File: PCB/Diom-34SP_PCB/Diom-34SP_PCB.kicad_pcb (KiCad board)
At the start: 2 copper layers, 119.9 x 95.5 mm, 19 parts, among them J1 Conn_01x02_Male, U1 nice_nano

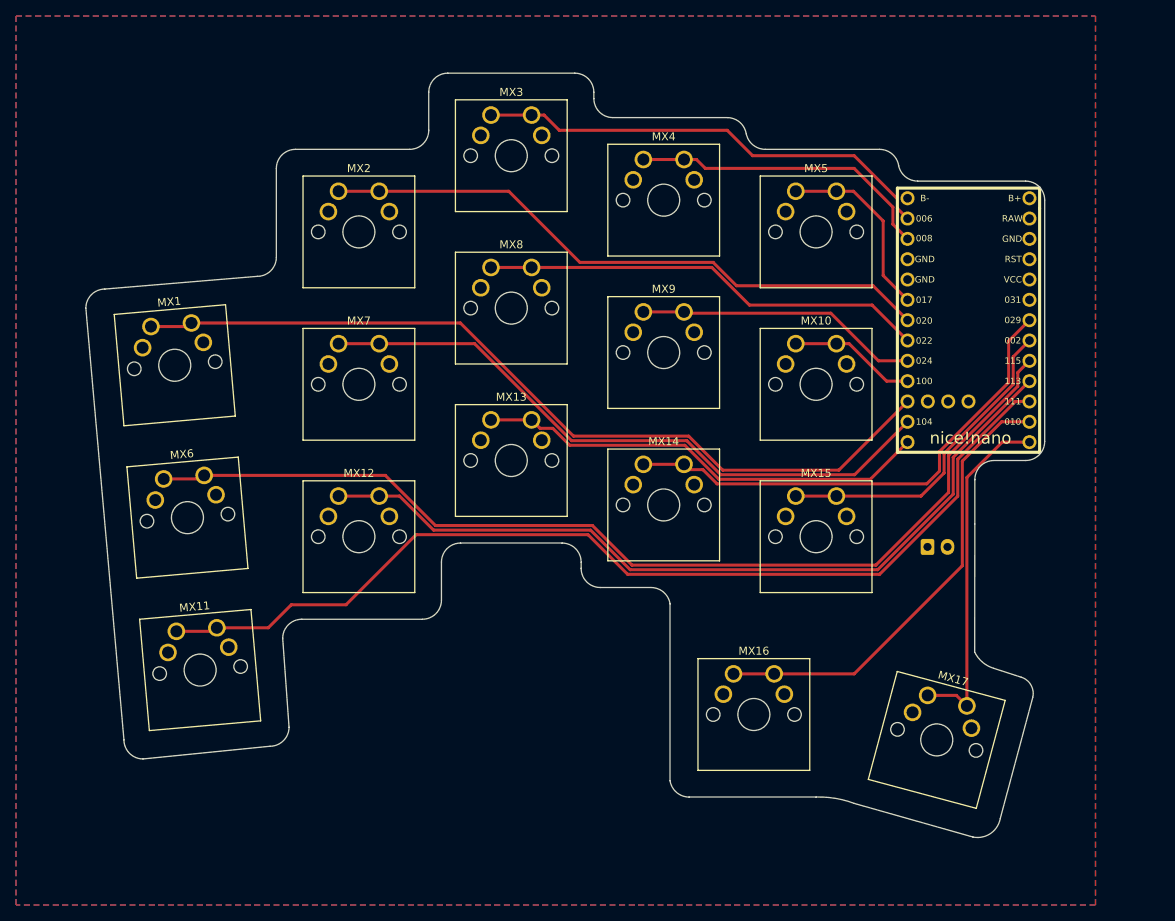
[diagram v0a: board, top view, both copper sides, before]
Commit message: Wired Battery Connector, 1.5U Thumb Key
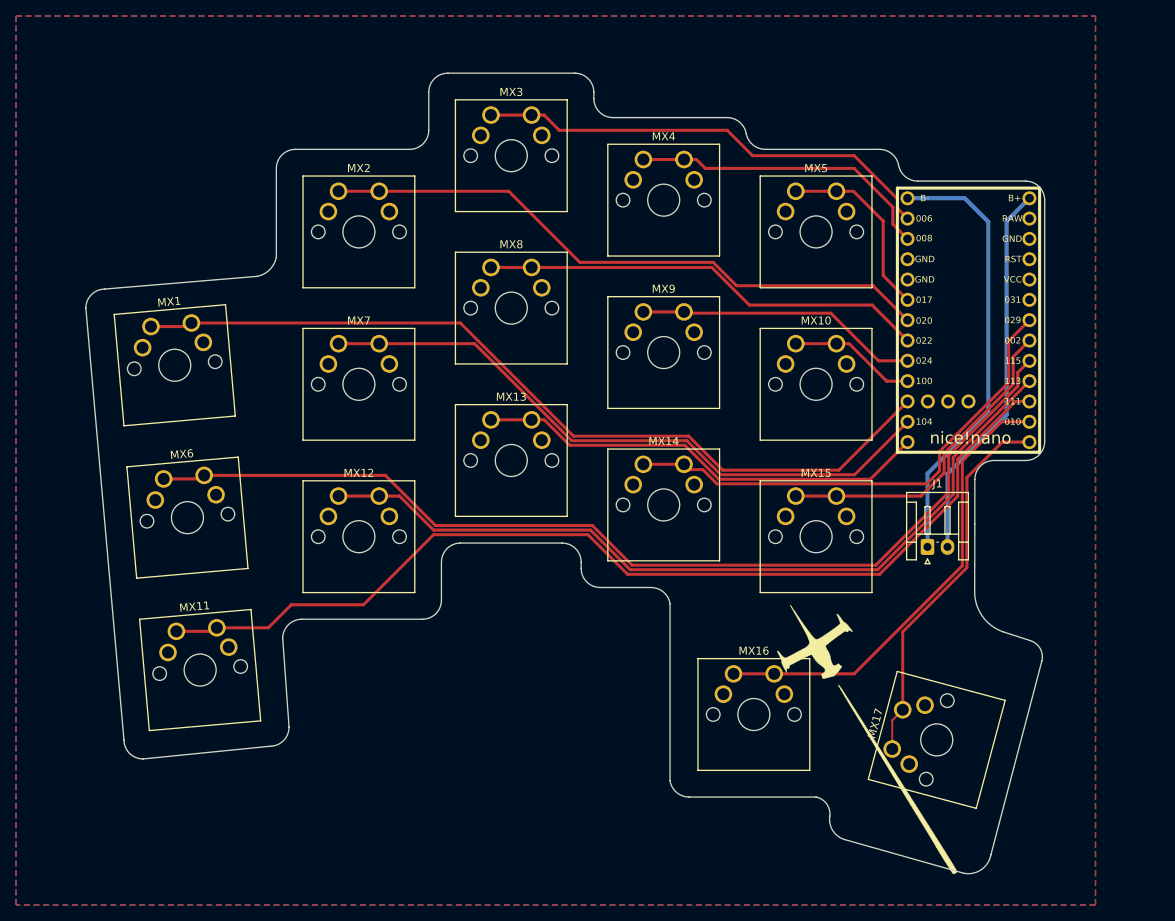
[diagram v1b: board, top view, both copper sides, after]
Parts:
- J1: moved to F.Cu
- MX17: footprint mx-switches-doubleSided:CherryMX-1U-doubleSided -> mx-switches-doubleSided:CherryMX-1.5U-doubleSided-Vertical
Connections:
- J1 pad 1: unconnected-(J1-Pad1) -> B-
- J1 pad 2: unconnected-(J1-Pad2) -> B+
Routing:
- net B-: track 0.00 -> 55.1 mm
- net B+: track 0.00 -> 47.8 mm
- net MX17: track 43.7 -> 47.5 mm
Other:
- board size 119.9 x 95.5 mm -> 119.9 x 100.1 mm

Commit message: Mounting Holes added
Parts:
- added H1: MountingHole, MountingHole:MountingHole_2.2mm_M2_DIN965, F.Cu at (70.6, 61.1)
- added H10: MountingHole, MountingHole:MountingHole_2.2mm_M2_DIN965, F.Cu at (198.9, 79.6)
- added H2: MountingHole, MountingHole:MountingHole_2.2mm_M2_DIN965, F.Cu at (75.4, 114.3)
- added H3: MountingHole, MountingHole:MountingHole_2.2mm_M2_DIN965, F.Cu at (193.5, 105.7)
- added H4: MountingHole, MountingHole:MountingHole_2.2mm_M2_DIN965, F.Cu at (187.2, 129.3)
- added H5: MountingHole, MountingHole:MountingHole_2.2mm_M2_DIN965, F.Cu at (137.5, 34.8)
- added H6: MountingHole, MountingHole:MountingHole_2.2mm_M2_DIN965, F.Cu at (118.2, 91.2)
- added H7: MountingHole, MountingHole:MountingHole_2.2mm_M2_DIN965, F.Cu at (175.6, 46.9)
- added H8: MountingHole, MountingHole:MountingHole_2.2mm_M2_DIN965, F.Cu at (175.6, 79.6)
- added H9: MountingHole, MountingHole:MountingHole_2.2mm_M2_DIN965, F.Cu at (198.9, 46.9)
- moved U1 4.69 mm to (187.2, 63.1)
- moved J1 0.95 mm to (177.8, 91.1)
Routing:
- net MX3: track 58.1 -> 63.2 mm
- net MX10: track 15.9 -> 20.6 mm
- net MX9: track 35.6 -> 40.2 mm
- net MX8: track 55.9 -> 60.5 mm
- net MX7: track 80.6 -> 85.3 mm
- net MX2: track 77.8 -> 82.5 mm
- net MX1: track 105.9 -> 110.6 mm
- net MX13: track 57.1 -> 61.8 mm
- net MX15: track 40.7 -> 44.6 mm
- net MX14: track 62.2 -> 66.1 mm
- net MX4: track 38.4 -> 41.8 mm
- net B-: track 55.1 -> 57.8 mm, vias 0 -> 1
- net MX12: track 102.6 -> 105.3 mm
- net MX6: track 127.3 -> 130.0 mm
- net B+: track 47.8 -> 50.5 mm, vias 0 -> 1
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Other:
- board size 119.9 x 100.1 mm -> 133.5 x 101.1 mm
